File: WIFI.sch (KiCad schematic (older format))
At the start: 38 parts, among them P601 ESP_DBG, P602 BT_DBG, P603 WL_DBG, P604 WL_RS232, U601 ESP-12E, U602 U.FL, U603 U.FL, U604 WL1807MOD, Y601 ANT1/BT, Y602 ANT2/WL

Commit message: Created netlist with current components Foreward Annotation to Board
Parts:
- C601, C602, C603, C606: footprint Capacitors_SMD:C_0603 -> Capacitors_SMD:C_0402
- L601, L602, L603, L604: footprint Resistors_SMD:R_0603 -> Choke_SMD:Choke_SMD_1206_Standard
- P601: footprint (none) -> Pin_Headers:Pin_Header_Straight_1x02
- R601, R605, R606, R607, R608: footprint Resistors_SMD:R_0603 -> Resistors_SMD:R_0402
- R602, R603, R604, R609, R610, R611, R612, R613, R614, R615, R616, R617, R618: footprint (none) -> Resistors_SMD:R_0402
- U601: footprint (none) -> NokiaRetroFit:ESP-12E
- U602, U603: footprint buttons:Foil_Button -> NokiaRetroFit:Foil_Button
- Y601, Y602: footprint (none) -> SMD_Packages:1Pin
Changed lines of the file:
@@
 F 0 "U601" H 5200 7600 50  0000 C CNN
 F 1 "ESP-12E" H 4700 7050 50  0000 C CNN
-F 2 "" H 4700 6950 50  0001 C CNN
+F 2 "NokiaRetroFit:ESP-12E" H 4700 6950 50  0001 C CNN
 F 3 "" H 4700 6950 50  0001 C CNN
 	1    4700 6950
@@
 F 0 "R601" V 3200 6350 50  0000 C CNN
 F 1 "0" V 3100 6350 50  0000 C CNN
-F 2 "Resistors_SMD:R_0603" V 3030 6350 50  0001 C CNN
+F 2 "Resistors_SMD:R_0402" V 3030 6350 50  0001 C CNN
 F 3 "" H 3100 6350 50  0000 C CNN
 	1    3100 6350
@@
 F 0 "C606" H 11875 9250 50  0000 L CNN
 F 1 "100n" H 11875 9050 50  0000 L CNN
-F 2 "Capacitors_SMD:C_0603" H 11888 9000 50  0001 C CNN
+F 2 "Capacitors_SMD:C_0402" H 11888 9000 50  0001 C CNN
 F 3 "" H 11850 9150 50  0000 C CNN
 	1    11850 9150
@@
 F 0 "Y602" H 11100 4350 60  0000 C CNN
 F 1 "ANT2/WL" H 11450 4250 60  0000 C CNN
-F 2 "" H 10850 4250 60  0001 C CNN
+F 2 "SMD_Packages:1Pin" H 10850 4250 60  0001 C CNN
 F 3 "" H 10850 4250 60  0000 C CNN
 	1    10850 4250
@@
 F 0 "Y601" H 11100 3450 60  0000 C CNN
 F 1 "ANT1/BT" H 11450 3350 60  0000 C CNN
-F 2 "" H 10850 3350 60  0001 C CNN
+F 2 "SMD_Packages:1Pin" H 10850 3350 60  0001 C CNN
 F 3 "" H 10850 3350 60  0000 C CNN
 F 4 "DNP" H 11400 3250 60  0000 C CNN "manufacture"
@@
 F 0 "L601" H 10930 3540 50  0000 L CNN
 F 1 "1n3" H 10930 3460 50  0000 L CNN
-F 2 "Resistors_SMD:R_0603" H 10900 3500 50  0001 C CNN
+F 2 "Choke_SMD:Choke_SMD_1206_Standard" H 10900 3500 50  0001 C CNN
 F 3 "" H 10900 3500 50  0000 C CNN
 F 4 "DNP" H 10900 3500 60  0000 C CNN "manufacture"
@@
 F 0 "L602" H 10930 4440 50  0000 L CNN
 F 1 "2n2" H 10930 4360 50  0000 L CNN
-F 2 "Resistors_SMD:R_0603" H 10900 4400 50  0001 C CNN
+F 2 "Choke_SMD:Choke_SMD_1206_Standard" H 10900 4400 50  0001 C CNN
 F 3 "" H 10900 4400 50  0000 C CNN
 	1    10900 4400
@@
 F 0 "L604" H 11230 4440 50  0000 L CNN
 F 1 "1n8" H 11230 4360 50  0000 L CNN
-F 2 "Resistors_SMD:R_0603" H 11200 4400 50  0001 C CNN
+F 2 "Choke_SMD:Choke_SMD_1206_Standard" H 11200 4400 50  0001 C CNN
 F 3 "" H 11200 4400 50  0000 C CNN
 	1    11200 4400
@@
 F 0 "L603" H 11230 3540 50  0000 L CNN
 F 1 "0" H 11230 3460 50  0000 L CNN
-F 2 "Resistors_SMD:R_0603" H 11200 3500 50  0001 C CNN
+F 2 "Choke_SMD:Choke_SMD_1206_Standard" H 11200 3500 50  0001 C CNN
 F 3 "" H 11200 3500 50  0000 C CNN
 F 4 "DNP" H 11200 3500 60  0000 C CNN "manufacture"
@@
 F 0 "C603" V 10950 4250 50  0000 C CNN
 F 1 "2p4" V 11000 4300 50  0000 L CNN
-F 2 "Capacitors_SMD:C_0603" H 11050 4250 50  0001 C CNN
+F 2 "Capacitors_SMD:C_0402" H 11050 4250 50  0001 C CNN
 F 3 "" H 11050 4250 50  0000 C CNN
 	1    11050 4250
@@
 F 0 "C602" V 10950 3350 50  0000 C CNN
 F 1 "1p" V 11000 3400 50  0000 L CNN
-F 2 "Capacitors_SMD:C_0603" H 11050 3350 50  0001 C CNN
+F 2 "Capacitors_SMD:C_0402" H 11050 3350 50  0001 C CNN
 F 3 "" H 11050 3350 50  0000 C CNN
 F 4 "DNP" V 11050 3350 60  0000 C CNN "manufacture"
@@
 F 0 "U603" H 12675 4950 60  0000 C CNN
 F 1 "U.FL" H 12575 4500 60  0000 C CNN
-F 2 "buttons:Foil_Button" H 12225 4750 60  0001 C CNN
+F 2 "NokiaRetroFit:Foil_Button" H 12225 4750 60  0001 C CNN
 F 3 "" H 12225 4750 60  0000 C CNN
 F 4 "DNP" H 12725 4525 60  0000 C CNN "manufacture"
@@
 F 0 "U602" H 12675 4050 60  0000 C CNN
 F 1 "U.FL" H 12575 3600 60  0000 C CNN
-F 2 "buttons:Foil_Button" H 12225 3850 60  0001 C CNN
+F 2 "NokiaRetroFit:Foil_Button" H 12225 3850 60  0001 C CNN
 F 3 "" H 12225 3850 60  0000 C CNN
 F 4 "DNP" H 12725 3625 60  0000 C CNN "manufacture"
@@
 F 0 "R605" V 12005 3350 50  0000 C CNN
 F 1 "0" V 11925 3350 50  0000 C CNN
-F 2 "Resistors_SMD:R_0603" V 11855 3350 50  0001 C CNN
+F 2 "Resistors_SMD:R_0402" V 11855 3350 50  0001 C CNN
 F 3 "" H 11925 3350 50  0000 C CNN
 F 4 "DNP" V 11925 3350 60  0000 C CNN "manufacture"
@@
 F 0 "R608" H 12175 4475 50  0000 L CNN
 F 1 "0" V 12125 4450 50  0000 C CNN
-F 2 "Resistors_SMD:R_0603" V 12055 4450 50  0001 C CNN
+F 2 "Resistors_SMD:R_0402" V 12055 4450 50  0001 C CNN
 F 3 "" H 12125 4450 50  0000 C CNN
 F 4 "DNP" H 12175 4400 60  0000 L CNN "manufacture"
@@
 F 0 "R606" V 12005 4250 50  0000 C CNN
 F 1 "0" V 11925 4250 50  0000 C CNN
-F 2 "Resistors_SMD:R_0603" V 11855 4250 50  0001 C CNN
+F 2 "Resistors_SMD:R_0402" V 11855 4250 50  0001 C CNN
 F 3 "" H 11925 4250 50  0000 C CNN
 F 4 "DNP" V 11925 4250 60  0000 C CNN "manufacture"
@@
 F 0 "R607" H 12175 3575 50  0000 L CNN
 F 1 "0" V 12125 3550 50  0000 C CNN
-F 2 "Resistors_SMD:R_0603" V 12055 3550 50  0001 C CNN
+F 2 "Resistors_SMD:R_0402" V 12055 3550 50  0001 C CNN
 F 3 "" H 12125 3550 50  0000 C CNN
 F 4 "DNP" H 12175 3500 60  0000 L CNN "manufacture"
@@
 F 0 "P601" H 6150 6850 50  0000 C CNN
 F 1 "ESP_DBG" V 6250 6700 50  0000 C CNN
-F 2 "" H 6150 6700 50  0000 C CNN
+F 2 "Pin_Headers:Pin_Header_Straight_1x02" H 6150 6700 50  0001 C CNN
 F 3 "" H 6150 6700 50  0000 C CNN
 	1    6150 6700
@@
 F 0 "C601" H 3125 7650 50  0000 L CNN
 F 1 "100n" H 3125 7450 50  0000 L CNN
-F 2 "Capacitors_SMD:C_0603" H 3138 7400 50  0001 C CNN
+F 2 "Capacitors_SMD:C_0402" H 3138 7400 50  0001 C CNN
 F 3 "" H 3100 7550 50  0000 C CNN
 	1    3100 7550
@@
 F 0 "R602" V 3380 1800 50  0000 C CNN
 F 1 "0" V 3300 1800 50  0000 C CNN
-F 2 "" V 3230 1800 50  0000 C CNN
+F 2 "Resistors_SMD:R_0402" V 3230 1800 50  0001 C CNN
 F 3 "" H 3300 1800 50  0000 C CNN
 	1    3300 1800
@@
 F 0 "R604" V 3980 1800 50  0000 C CNN
 F 1 "0" V 3900 1800 50  0000 C CNN
-F 2 "" V 3830 1800 50  0000 C CNN
+F 2 "Resistors_SMD:R_0402" V 3830 1800 50  0001 C CNN
 F 3 "" H 3900 1800 50  0000 C CNN
 F 4 "DNP" V 3900 1800 60  0000 C CNN "manufacture"
@@
 F 0 "R618" V 14330 1000 50  0000 C CNN
 F 1 "100k" V 14250 1000 50  0000 C CNN
-F 2 "" V 14180 1000 50  0000 C CNN
+F 2 "Resistors_SMD:R_0402" V 14180 1000 50  0001 C CNN
 F 3 "" H 14250 1000 50  0000 C CNN
 F 4 "DNP" V 14250 1000 60  0000 C CNN "manufacture"
@@
 F 0 "R603" V 3680 8950 50  0000 C CNN
 F 1 "100k" V 3600 8950 50  0000 C CNN
-F 2 "" V 3530 8950 50  0000 C CNN
+F 2 "Resistors_SMD:R_0402" V 3530 8950 50  0001 C CNN
 F 3 "" H 3600 8950 50  0000 C CNN
 	1    3600 8950
@@
 F 0 "R610" V 13750 1600 50  0000 C CNN
 F 1 "0" V 13800 1400 50  0000 C CNN
-F 2 "" V 13730 1400 50  0000 C CNN
+F 2 "Resistors_SMD:R_0402" V 13730 1400 50  0001 C CNN
 F 3 "" H 13800 1400 50  0000 C CNN
 F 4 "DNP" V 13800 1400 60  0000 C CNN "manufacture"
@@
 F 0 "R609" V 13750 1500 50  0000 C CNN
 F 1 "0" V 13800 1300 50  0000 C CNN
-F 2 "" V 13730 1300 50  0000 C CNN
+F 2 "Resistors_SMD:R_0402" V 13730 1300 50  0001 C CNN
 F 3 "" H 13800 1300 50  0000 C CNN
 F 4 "DNP" V 13800 1300 60  0000 C CNN "manufacture"
@@
 F 0 "R611" V 13750 1700 50  0000 C CNN
 F 1 "0" V 13800 1500 50  0000 C CNN
-F 2 "" V 13730 1500 50  0000 C CNN
+F 2 "Resistors_SMD:R_0402" V 13730 1500 50  0001 C CNN
 F 3 "" H 13800 1500 50  0000 C CNN
 F 4 "DNP" V 13800 1500 60  0000 C CNN "manufacture"
@@
 F 0 "R612" V 13750 1800 50  0000 C CNN
 F 1 "0" V 13800 1600 50  0000 C CNN
-F 2 "" V 13730 1600 50  0000 C CNN
+F 2 "Resistors_SMD:R_0402" V 13730 1600 50  0001 C CNN
 F 3 "" H 13800 1600 50  0000 C CNN
 F 4 "DNP" V 13800 1600 60  0000 C CNN "manufacture"
@@
 F 0 "R614" V 13750 2000 50  0000 C CNN
 F 1 "0" V 13800 1800 50  0000 C CNN
-F 2 "" V 13730 1800 50  0000 C CNN
+F 2 "Resistors_SMD:R_0402" V 13730 1800 50  0001 C CNN
 F 3 "" H 13800 1800 50  0000 C CNN
 F 4 "DNP" V 13800 1800 60  0000 C CNN "manufacture"
@@
 F 0 "R613" V 13750 1900 50  0000 C CNN
 F 1 "0" V 13800 1700 50  0000 C CNN
-F 2 "" V 13730 1700 50  0000 C CNN
+F 2 "Resistors_SMD:R_0402" V 13730 1700 50  0001 C CNN
 F 3 "" H 13800 1700 50  0000 C CNN
 F 4 "DNP" V 13800 1700 60  0000 C CNN "manufacture"
@@
 F 0 "R615" V 13750 2100 50  0000 C CNN
 F 1 "0" V 13800 1900 50  0000 C CNN
-F 2 "" V 13730 1900 50  0000 C CNN
+F 2 "Resistors_SMD:R_0402" V 13730 1900 50  0001 C CNN
 F 3 "" H 13800 1900 50  0000 C CNN
 F 4 "DNP" V 13800 1900 60  0000 C CNN "manufacture"
@@
 F 0 "R616" V 13750 2200 50  0000 C CNN
 F 1 "0" V 13800 2000 50  0000 C CNN
-F 2 "" V 13730 2000 50  0000 C CNN
+F 2 "Resistors_SMD:R_0402" V 13730 2000 50  0001 C CNN
 F 3 "" H 13800 2000 50  0000 C CNN
 F 4 "DNP" V 13800 2000 60  0000 C CNN "manufacture"
@@
 F 0 "R617" V 13750 2300 50  0000 C CNN
 F 1 "0" V 13800 2100 50  0000 C CNN
-F 2 "" V 13730 2100 50  0000 C CNN
+F 2 "Resistors_SMD:R_0402" V 13730 2100 50  0001 C CNN
 F 3 "" H 13800 2100 50  0000 C CNN
 F 4 "DNP" V 13800 2100 60  0000 C CNN "manufacture"

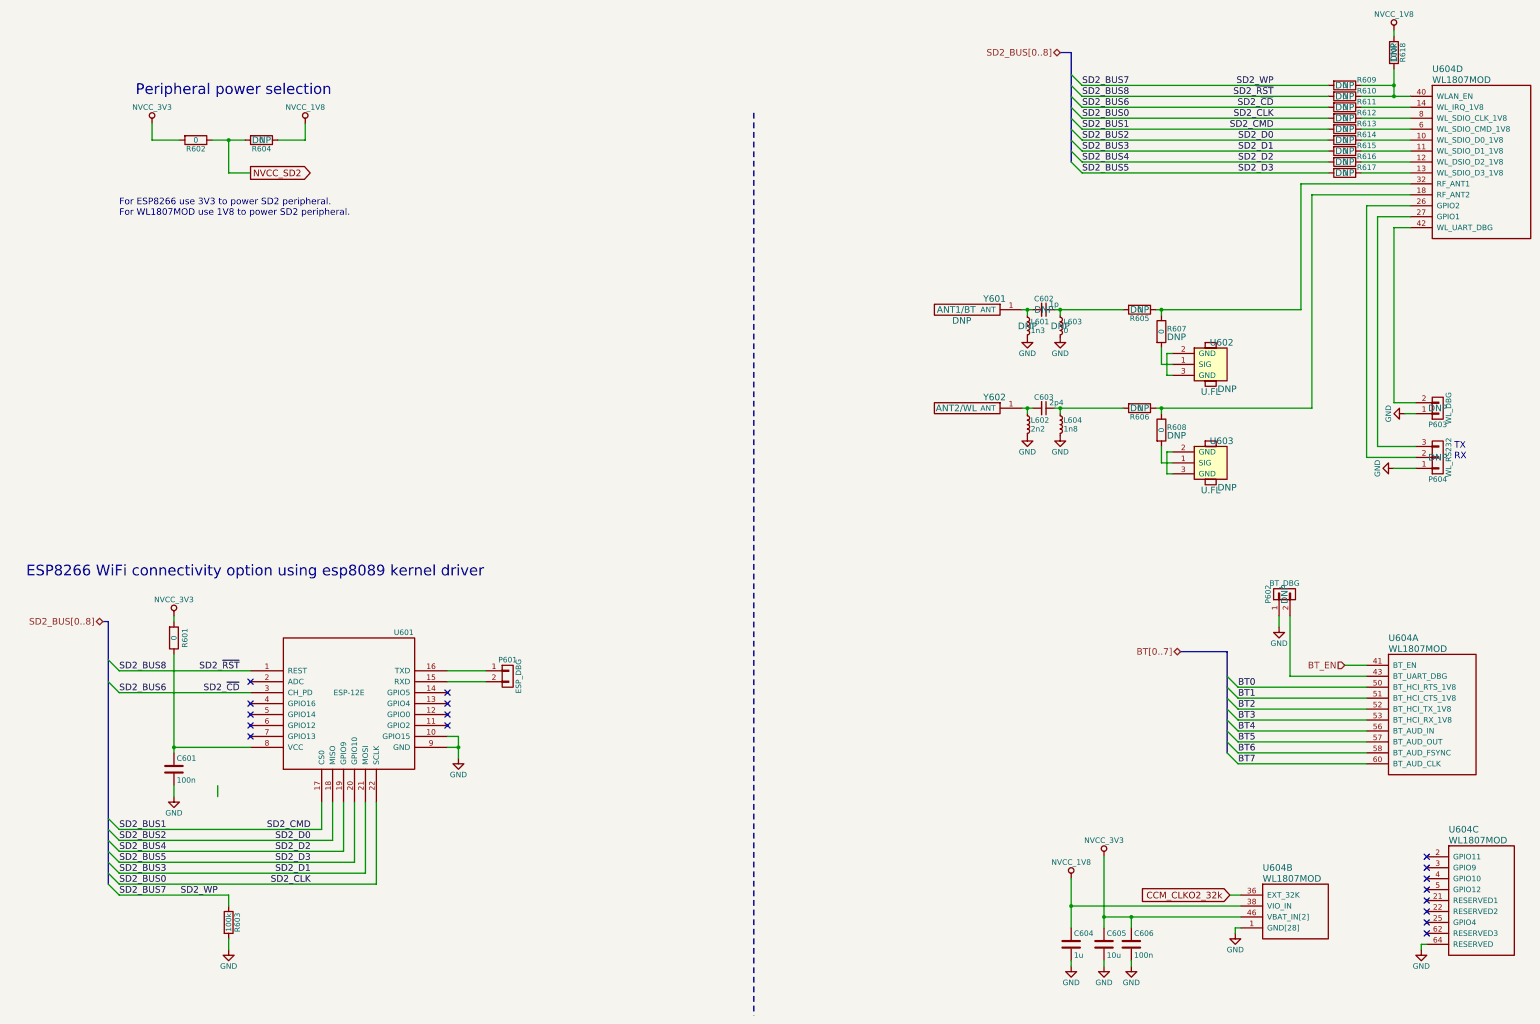
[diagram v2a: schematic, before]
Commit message: Modification for STM32 adaption
For the Hackaday Prize 2017 I decided to switch to STM32 as CPU

*Power system was modified to just contain the charge IC,
*Boost converter for high voltage peripherals
*Buck converter for 3V3 for CPU and switchable NVCC_3V3
   for peripherie

CPU signals are routed and pinmux is done in firmware folder.

SD-Card has 4bit Interface

WiFi module ESP8266 is connected via UART

Wolfson Ausio codec is connected via SAI

Two digital microphones for noise canceling

Rumble Motor driver

LCD is connected via it's own I2C interface
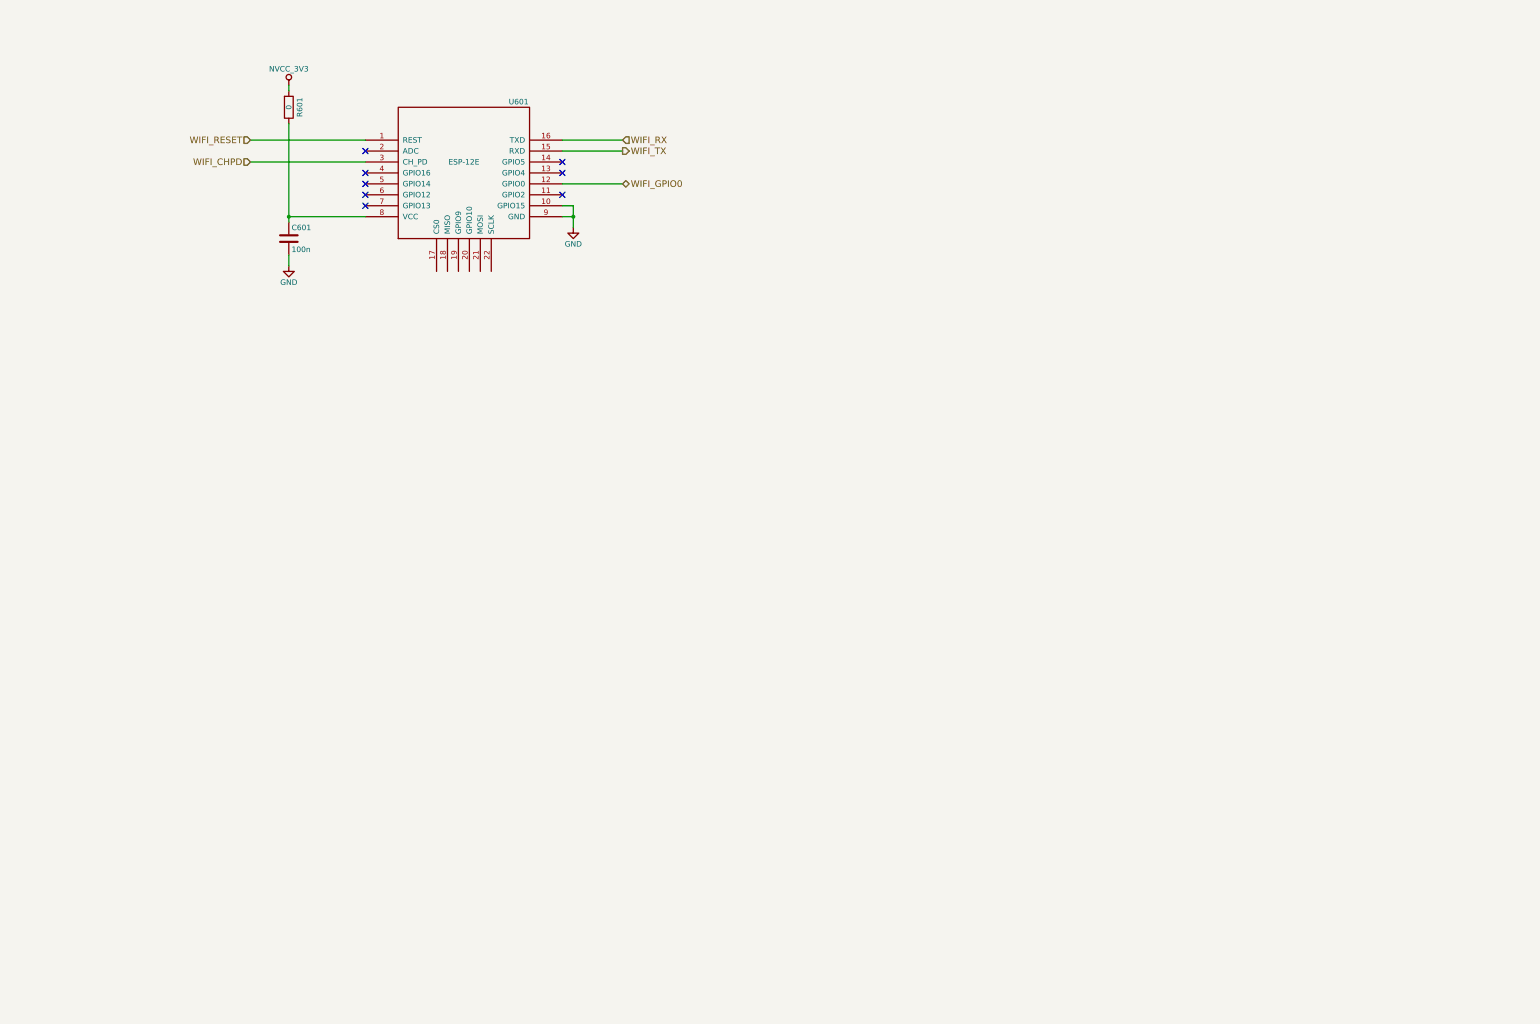
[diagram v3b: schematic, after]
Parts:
- removed C602: 1p, Capacitors_SMD:C_0402, symbol C_Small
- removed C603: 2p4, Capacitors_SMD:C_0402, symbol C_Small
- removed C604: 1u, Capacitors_SMD:C_0603, symbol C
- removed C605: 10u, Capacitors_SMD:C_0603, symbol C
- removed C606: 100n, Capacitors_SMD:C_0402, symbol C
- removed L601: 1n3, Choke_SMD:Choke_SMD_1206_Standard, symbol L_Small
- removed L602: 2n2, Choke_SMD:Choke_SMD_1206_Standard, symbol L_Small
- removed L603: 0, Choke_SMD:Choke_SMD_1206_Standard, symbol L_Small
- removed L604: 1n8, Choke_SMD:Choke_SMD_1206_Standard, symbol L_Small
- removed P601: ESP_DBG, Pin_Headers:Pin_Header_Straight_1x02, symbol CONN_01X02
- removed P602: BT_DBG, Pin_Headers:Pin_Header_Straight_1x02, symbol CONN_01X02
- removed P603: WL_DBG, Pin_Headers:Pin_Header_Straight_1x02, symbol CONN_01X02
- removed P604: WL_RS232, Pin_Headers:Pin_Header_Straight_1x03, symbol CONN_01X03
- removed R602, R604, R605, R606, R607, R608, R609, R610, R611, R612, R613, R614, R615, R616, R617: 0, Resistors_SMD:R_0402, symbol R
- removed R603, R618: 100k, Resistors_SMD:R_0402, symbol R
- removed U602, U603: U.FL, NokiaRetroFit:Foil_Button, symbol U.FL
- removed U604: WL1807MOD, symbol WL1807MOD
- removed Y601: ANT1/BT, SMD_Packages:1Pin, symbol W3006
- removed Y602: ANT2/WL, SMD_Packages:1Pin, symbol W3006
- C601: footprint Capacitors_SMD:C_0402 -> Capacitors_SMD:C_0402_NoSilk
- R601: footprint Resistors_SMD:R_0402 -> Resistors_SMD:R_0402_NoSilk
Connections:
- net WIFI_GPIO0: now reaches U601.12 (GPIO0)
- net WIFI_TX: now reaches U601.15 (RXD)
- net WIFI_RX: now reaches U601.16 (TXD)
- net SD2_BUS0: no longer names the net of U601.22 (SCLK)
- net SD2_BUS1: no longer names the net of U601.17 (CS0)
- net SD2_BUS2: no longer names the net of U601.18 (MISO)
- net SD2_BUS3: no longer names the net of U601.21 (MOSI)
- net SD2_BUS4: no longer names the net of U601.19 (GPIO9)
- net SD2_BUS5: no longer names the net of U601.20 (GPIO10)
- net SD2_BUS6 renamed WIFI_CHPD
- net SD2_BUS8 renamed WIFI_RESET
- no-connect marks 17 -> 8
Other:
- note removed: "ESP8266 WiFi connectivity option using esp8089 kernel driver"
- note removed: "For ESP8266 use 3V3 to power SD2 peripheral.\nFor WL1807MOD use 1V8 to power SD2 peripheral."
- note removed: "Peripheral power selection"
- note removed: "TX\nRX"
- moved on the sheet: C601, R601, U601
